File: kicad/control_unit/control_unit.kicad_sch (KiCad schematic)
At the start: 50 parts

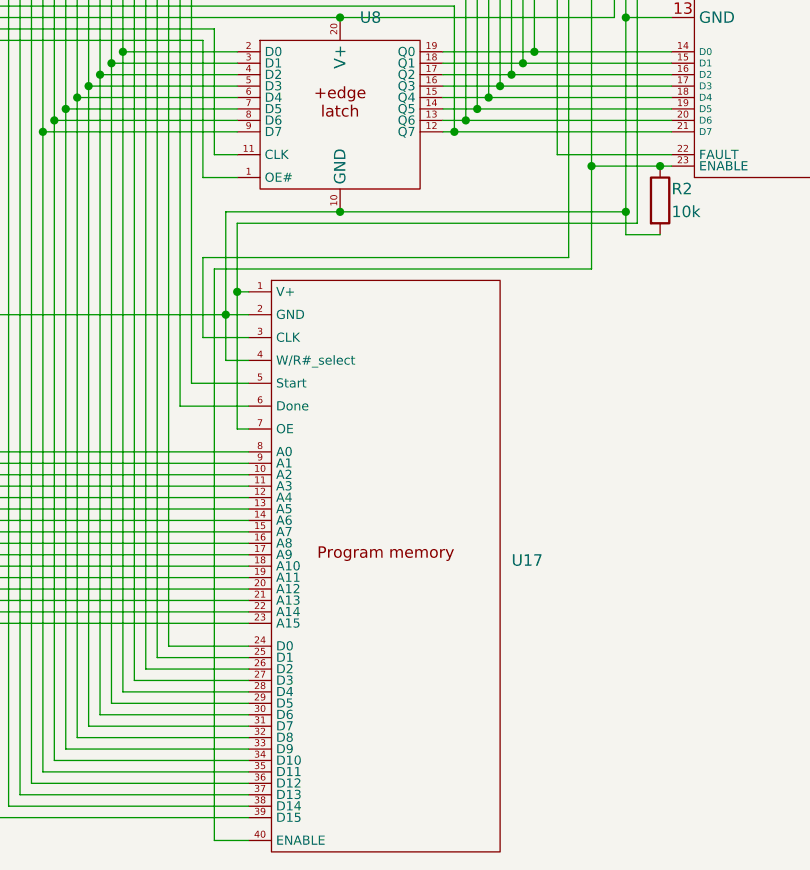
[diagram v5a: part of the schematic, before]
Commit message: Finished prog memory timing diagrams
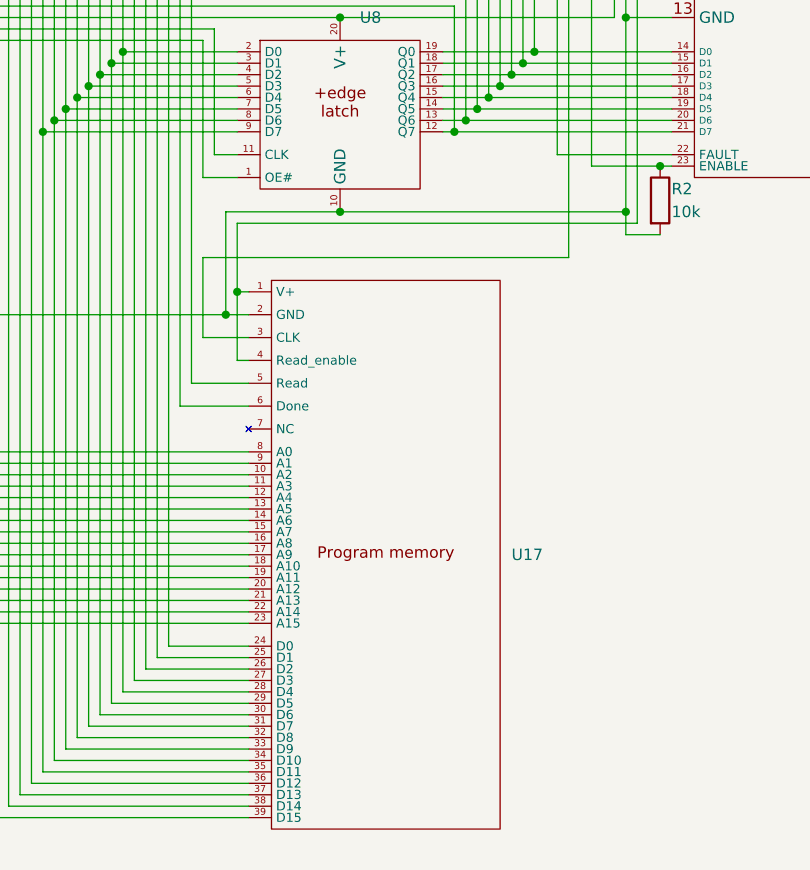
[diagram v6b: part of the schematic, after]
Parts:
- U17: value ~ -> (none); footprint Connector_PinHeader_2.54mm:PinHeader_1x40_P2.54mm_Vertical -> Connector_PinHeader_2.54mm:PinHeader_1x39_P2.54mm_Vertical; symbol custom_symbol_lib:prog_mem_interface -> custom_symbol_lib:prog_mem_interface_read
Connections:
- net at R10.1, R11.1, R12.1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: now also U17.4 (Read_enable); no longer U17.7 (OE)
- net at D1.1 (K), D2.1 (K), D3.1 (K)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: no longer U17.4 (W/R#_select)
- net at R2.1, U1.23 (ENABLE), U12.1 (1A)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: no longer U17.40 (ENABLE)
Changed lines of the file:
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@@
 	)
 	(junction
+		(at 299.72 184.15)
+		(diameter 0)
+		(color 0 0 0 0)
+	)
+	(junction
 		(at 217.17 121.92)
 		(diameter 0)
@@
 	)
 	(junction
-		(at 299.72 184.15)
-		(diameter 0)
-		(color 0 0 0 0)
-	)
-	(junction
 		(at 236.22 165.1)
 		(diameter 0)
@@
 	)
 	(junction
-		(at 339.09 170.18)
-		(diameter 0)
-		(color 0 0 0 0)
-	)
-	(junction
 		(at 124.46 214.63)
 		(diameter 0)
@@
 	(wire
 		(pts
-			(xy 339.09 181.61) (xy 297.18 181.61)
-		)
-		(stroke
-			(width 0)
-			(type default)
-		)
-	)
-	(wire
-		(pts
 			(xy 302.26 130.81) (xy 302.26 132.08)
 		)
@@
 	(wire
 		(pts
-			(xy 299.72 184.15) (xy 299.72 199.39)
-		)
-		(stroke
-			(width 0)
-			(type default)
-		)
-	)
-	(wire
-		(pts
 			(xy 261.62 210.82) (xy 300.99 210.82)
 		)
@@
 	(wire
 		(pts
-			(xy 339.09 170.18) (xy 339.09 181.61)
-		)
-		(stroke
-			(width 0)
-			(type default)
-		)
-	)
-	(wire
-		(pts
 			(xy 111.76 186.69) (xy 71.12 186.69)
 		)
@@
 	(wire
 		(pts
-			(xy 298.45 191.77) (xy 298.45 186.69)
-		)
-		(stroke
-			(width 0)
-			(type default)
-		)
-	)
-	(wire
-		(pts
 			(xy 316.23 93.98) (xy 327.66 93.98)
 		)
@@
 	(wire
 		(pts
-			(xy 297.18 181.61) (xy 297.18 245.11)
-		)
-		(stroke
-			(width 0)
-			(type default)
-		)
-	)
-	(wire
-		(pts
 			(xy 254 218.44) (xy 254 223.52)
 		)
@@
 	(wire
 		(pts
-			(xy 297.18 245.11) (xy 300.99 245.11)
-		)
-		(stroke
-			(width 0)
-			(type default)
-		)
-	)
-	(wire
-		(pts
 			(xy 335.28 121.92) (xy 335.28 124.46)
 		)
@@
 	(wire
 		(pts
-			(xy 300.99 191.77) (xy 298.45 191.77)
-		)
-		(stroke
-			(width 0)
-			(type default)
-		)
-	)
-	(wire
-		(pts
 			(xy 87.63 194.31) (xy 100.33 194.31)
 		)
@@
 	(wire
 		(pts
-			(xy 199.39 121.92) (xy 191.77 121.92)
+			(xy 299.72 184.15) (xy 299.72 191.77)
 		)
 		(stroke
@@
 	(wire
 		(pts
-			(xy 213.36 203.2) (xy 220.98 203.2)
+			(xy 199.39 121.92) (xy 191.77 121.92)
 		)
 		(stroke
@@
 	(wire
 		(pts
-			(xy 77.47 214.63) (xy 77.47 236.22)
+			(xy 213.36 203.2) (xy 220.98 203.2)
 		)
 		(stroke
@@
 	(wire
 		(pts
-			(xy 300.99 199.39) (xy 299.72 199.39)
+			(xy 77.47 214.63) (xy 77.47 236.22)
 		)
 		(stroke
@@
 	(wire
 		(pts
+			(xy 299.72 191.77) (xy 300.99 191.77)
+		)
+		(stroke
+			(width 0)
+			(type default)
+		)
+	)
+	(wire
+		(pts
 			(xy 201.93 96.52) (xy 140.97 96.52)
 		)
@@
 	)
 	(symbol
-		(lib_id "custom_symbol_lib:prog_mem_interface")
+		(lib_id "custom_symbol_lib:prog_mem_interface_read")
 		(at 316.23 214.63 0)
 		(unit 1)
@@
 		(fields_autoplaced yes)
 		(property "Reference" "U17"
-			(at 330.2 213.9949 0)
+			(at 330.2 213.3599 0)
 			(effects
 				(font
@@
 			)
 		)
-		(property "Value" "~"
-			(at 330.2 215.9 0)
+		(property "Value" ""
+			(at 303.53 204.47 0)
 			(effects
 				(font
 					(size 1.27 1.27)
 				)
-				(justify left)
 			)
 		)
-		(property "Footprint" "Connector_PinHeader_2.54mm:PinHeader_1x40_P2.54mm_Vertical"
-			(at 316.23 247.65 0)
+		(property "Footprint" "Connector_PinHeader_2.54mm:PinHeader_1x39_P2.54mm_Vertical"
+			(at 316.23 245.872 0)
 			(effects
 				(font
@@
 		(pin "12"
 		)
-		(pin "40"
-		)
 		(instances
